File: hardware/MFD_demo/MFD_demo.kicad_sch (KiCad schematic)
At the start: 52 parts, among them J1 Pins_Ard, J2 POWER, Q1 IRF740, Q10 IRF740, Q2 IRF740, Q3 IRF740, Q4 IRF740, Q5 IRF740, Q6 IRF740, Q7 IRF740, Q8 IRF740, Q9 IRF740

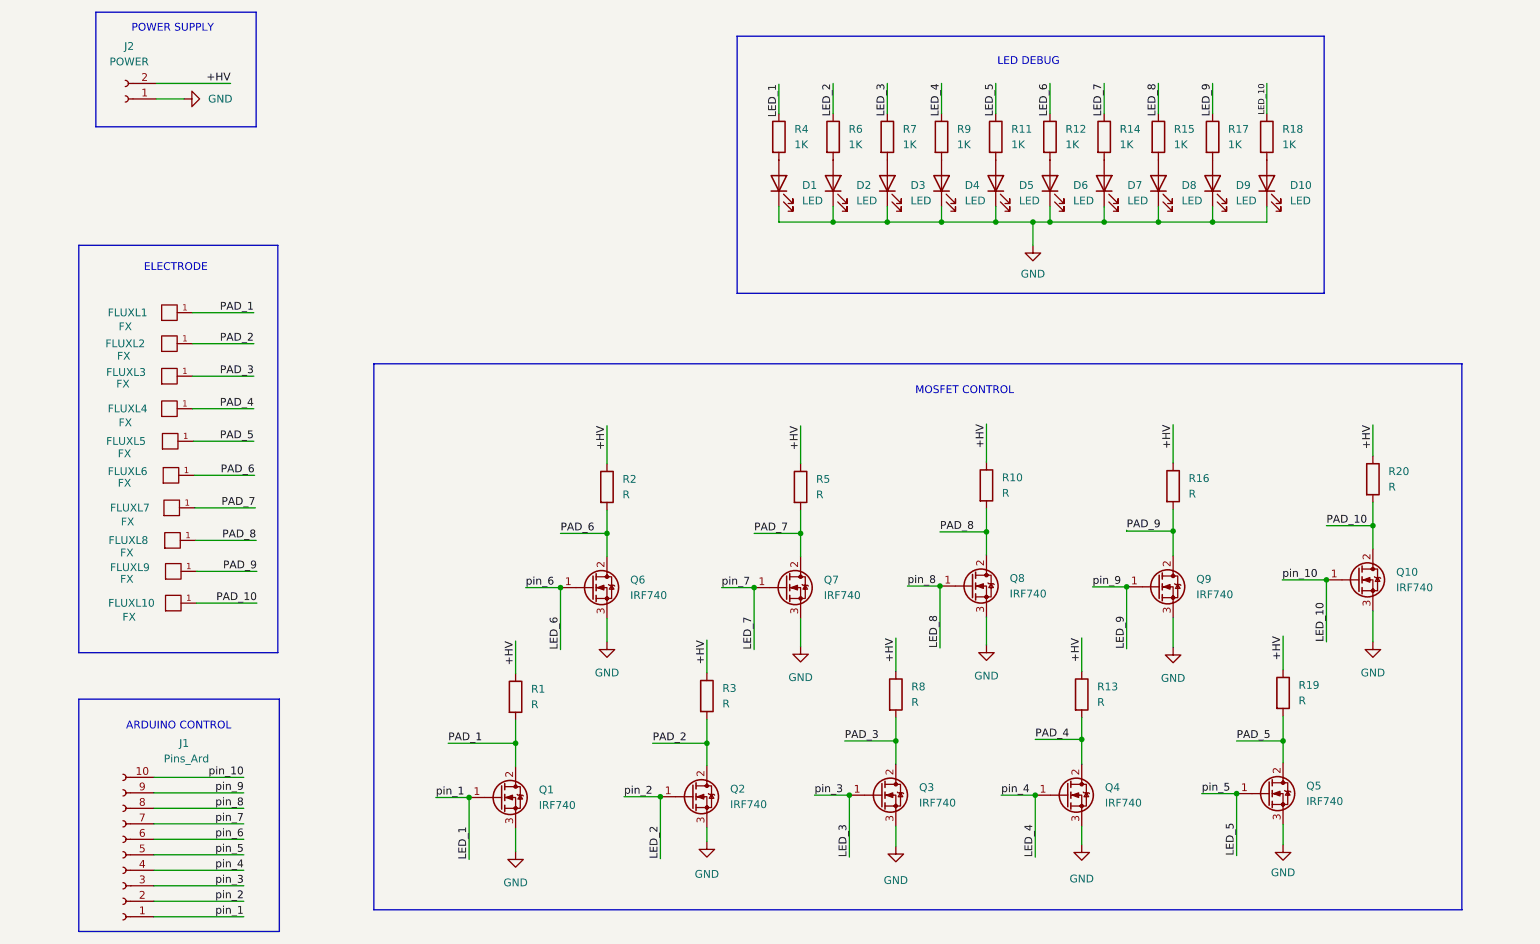
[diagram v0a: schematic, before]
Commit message: Update schem + layout PCB: Changes from 10 electrodes -> 6 electrodes
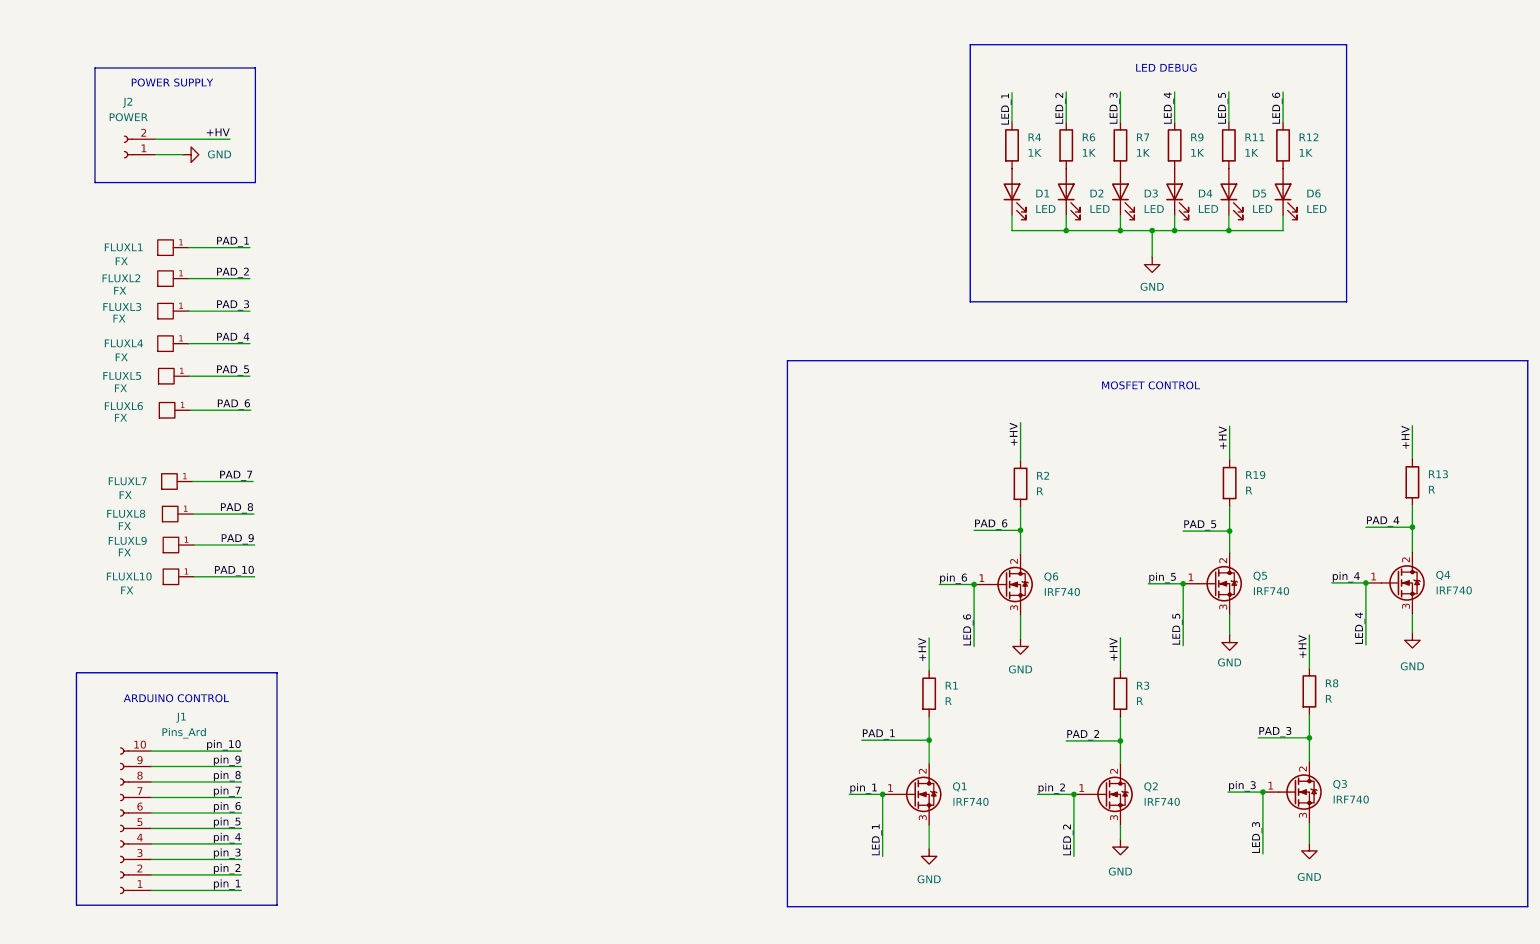
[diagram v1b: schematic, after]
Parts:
- removed D10, D7, D8, D9: LED, LED_THT:LED_D4.0mm, symbol Device:LED
- removed Q10, Q7, Q8, Q9: IRF740, Package_TO_SOT_THT:TO-220-3_Vertical, symbol Transistor_FET:IRF740
- removed R10, R16, R20, R5: R, Resistor_THT:R_Axial_DIN0207_L6.3mm_D2.5mm_P10.16mm_Horizontal, symbol Device:R
- removed R14, R15, R17, R18: 1K, Resistor_THT:R_Axial_DIN0207_L6.3mm_D2.5mm_P10.16mm_Horizontal, symbol Device:R
- D1, D2, D3, D4, D5, D6: footprint LED_THT:LED_D4.0mm -> LED_THT:LED_D5.0mm_IRBlack
- R1, R11, R12, R13, R19, R2, R3, R4, R6, R7, R8, R9: footprint Resistor_THT:R_Axial_DIN0207_L6.3mm_D2.5mm_P10.16mm_Horizontal -> Resistor_THT:R_Axial_DIN0204_L3.6mm_D1.6mm_P5.08mm_Horizontal
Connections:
- net LED_10 renamed pin_10
- net LED_7 renamed pin_7
- net LED_8 renamed pin_8
- net LED_9 renamed pin_9
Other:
- note removed: "ELECTRODE"
- moved on the sheet: D1, D2, D3, D4, D5, D6, FLUXL1, FLUXL10, FLUXL2, FLUXL3, FLUXL4, FLUXL5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

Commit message: Update PCB layout version 01
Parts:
- removed J1: Pins_Ard, Connector_PinHeader_2.54mm:PinHeader_1x10_P2.54mm_Vertical, symbol Connector:Conn_01x10_Female
- added J1, J3: GND_Electrodes, Connector_PinSocket_2.54mm:PinSocket_1x01_P2.54mm_Vertical, symbol Connector:Conn_01x01_Female
- added J10: GND, Connector_PinSocket_2.54mm:PinSocket_1x03_P2.54mm_Vertical, symbol Connector:Conn_01x03_Female
- added J4: Ard_1, Connector_PinSocket_2.54mm:PinSocket_1x01_P2.54mm_Vertical, symbol Connector:Conn_01x01_Female
- added J5: Ard_2, Connector_PinSocket_2.54mm:PinSocket_1x01_P2.54mm_Vertical, symbol Connector:Conn_01x01_Female
- added J6: Ard_3, Connector_PinSocket_2.54mm:PinSocket_1x01_P2.54mm_Vertical, symbol Connector:Conn_01x01_Female
- added J7: Ard_4, Connector_PinSocket_2.54mm:PinSocket_1x01_P2.54mm_Vertical, symbol Connector:Conn_01x01_Female
- added J8: Ard_5, Connector_PinSocket_2.54mm:PinSocket_1x01_P2.54mm_Vertical, symbol Connector:Conn_01x01_Female
- added J9: Ard_6, Connector_PinSocket_2.54mm:PinSocket_1x01_P2.54mm_Vertical, symbol Connector:Conn_01x01_Female
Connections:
- net PAD_8 is gone; now on an unnamed net: FLUXL8.1
- net PAD_9 is gone; now on an unnamed net: FLUXL9.1
- net GND: now also J10.1 (Pin_1), J10.2 (Pin_2), J10.3 (Pin_3)
- net LED_1: now also J4.1 (Pin_1)
- net LED_2: now also J5.1 (Pin_1)
- net LED_3: now also J6.1 (Pin_1)
- net LED_4: now also J7.1 (Pin_1)
- net LED_5: now also J8.1 (Pin_1)
- net LED_6: now also J9.1 (Pin_1)
- net PAD_10: no longer names the net of FLUXL10.1
- net PAD_10: now also J3.1 (Pin_1)
- net PAD_7: no longer names the net of FLUXL7.1
- net PAD_7: now also J1.1 (Pin_1)
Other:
- note added: "ELECTRODES"
- moved on the sheet: D1, D2, D3, D4, D5, D6, FLUXL1, FLUXL10, FLUXL2, FLUXL3, FLUXL4, FLUXL5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

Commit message: Update PCB layout
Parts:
- R1, R11, R12, R13, R19, R2, R3, R4, R6, R7, R8, R9: footprint Resistor_THT:R_Axial_DIN0204_L3.6mm_D1.6mm_P5.08mm_Horizontal -> Resistor_THT:R_Axial_DIN0207_L6.3mm_D2.5mm_P10.16mm_Horizontal
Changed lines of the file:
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@@
       (effects (font (size 1.27 1.27)) (justify left))
     )
-    (property "Footprint" "Resistor_THT:R_Axial_DIN0204_L3.6mm_D1.6mm_P5.08mm_Horizontal" (id 2) (at 169.545 128.905 90)
+    (property "Footprint" "Resistor_THT:R_Axial_DIN0207_L6.3mm_D2.5mm_P10.16mm_Horizontal" (id 2) (at 169.545 128.905 90)
       (effects (font (size 1.27 1.27)) hide)
     )
@@
       (effects (font (size 1.27 1.27)) (justify left))
     )
-    (property "Footprint" "Resistor_THT:R_Axial_DIN0204_L3.6mm_D1.6mm_P5.08mm_Horizontal" (id 2) (at 154.051 94.107 90)
+    (property "Footprint" "Resistor_THT:R_Axial_DIN0207_L6.3mm_D2.5mm_P10.16mm_Horizontal" (id 2) (at 154.051 94.107 90)
       (effects (font (size 1.27 1.27)) hide)
     )
@@
       (effects (font (size 1.27 1.27)) (justify left))
     )
-    (property "Footprint" "Resistor_THT:R_Axial_DIN0204_L3.6mm_D1.6mm_P5.08mm_Horizontal" (id 2) (at 203.962 128.905 90)
+    (property "Footprint" "Resistor_THT:R_Axial_DIN0207_L6.3mm_D2.5mm_P10.16mm_Horizontal" (id 2) (at 203.962 128.905 90)
       (effects (font (size 1.27 1.27)) hide)
     )
@@
       (effects (font (size 1.27 1.27)) (justify left))
     )
-    (property "Footprint" "Resistor_THT:R_Axial_DIN0204_L3.6mm_D1.6mm_P5.08mm_Horizontal" (id 2) (at 189.357 94.107 90)
+    (property "Footprint" "Resistor_THT:R_Axial_DIN0207_L6.3mm_D2.5mm_P10.16mm_Horizontal" (id 2) (at 189.357 94.107 90)
       (effects (font (size 1.27 1.27)) hide)
     )
@@
       (effects (font (size 1.27 1.27)) (justify left))
     )
-    (property "Footprint" "Resistor_THT:R_Axial_DIN0204_L3.6mm_D1.6mm_P5.08mm_Horizontal" (id 2) (at 181.356 41.402 90)
+    (property "Footprint" "Resistor_THT:R_Axial_DIN0207_L6.3mm_D2.5mm_P10.16mm_Horizontal" (id 2) (at 181.356 41.402 90)
       (effects (font (size 1.27 1.27)) hide)
     )
@@
       (effects (font (size 1.27 1.27)) (justify left))
     )
-    (property "Footprint" "Resistor_THT:R_Axial_DIN0204_L3.6mm_D1.6mm_P5.08mm_Horizontal" (id 2) (at 154.686 41.402 90)
+    (property "Footprint" "Resistor_THT:R_Axial_DIN0207_L6.3mm_D2.5mm_P10.16mm_Horizontal" (id 2) (at 154.686 41.402 90)
       (effects (font (size 1.27 1.27)) hide)
     )
@@
       (effects (font (size 1.27 1.27)) (justify left))
     )
-    (property "Footprint" "Resistor_THT:R_Axial_DIN0204_L3.6mm_D1.6mm_P5.08mm_Horizontal" (id 2) (at 223.647 94.107 90)
+    (property "Footprint" "Resistor_THT:R_Axial_DIN0207_L6.3mm_D2.5mm_P10.16mm_Horizontal" (id 2) (at 223.647 94.107 90)
       (effects (font (size 1.27 1.27)) hide)
     )
@@
       (effects (font (size 1.27 1.27)) (justify left))
     )
-    (property "Footprint" "Resistor_THT:R_Axial_DIN0204_L3.6mm_D1.6mm_P5.08mm_Horizontal" (id 2) (at 172.466 41.402 90)
+    (property "Footprint" "Resistor_THT:R_Axial_DIN0207_L6.3mm_D2.5mm_P10.16mm_Horizontal" (id 2) (at 172.466 41.402 90)
       (effects (font (size 1.27 1.27)) hide)
     )
@@
       (effects (font (size 1.27 1.27)) (justify left))
     )
-    (property "Footprint" "Resistor_THT:R_Axial_DIN0204_L3.6mm_D1.6mm_P5.08mm_Horizontal" (id 2) (at 136.906 41.402 90)
+    (property "Footprint" "Resistor_THT:R_Axial_DIN0207_L6.3mm_D2.5mm_P10.16mm_Horizontal" (id 2) (at 136.906 41.402 90)
       (effects (font (size 1.27 1.27)) hide)
     )
@@
       (effects (font (size 1.27 1.27)) (justify left))
     )
-    (property "Footprint" "Resistor_THT:R_Axial_DIN0204_L3.6mm_D1.6mm_P5.08mm_Horizontal" (id 2) (at 137.16 128.524 90)
+    (property "Footprint" "Resistor_THT:R_Axial_DIN0207_L6.3mm_D2.5mm_P10.16mm_Horizontal" (id 2) (at 137.16 128.524 90)
       (effects (font (size 1.27 1.27)) hide)
     )
@@
       (effects (font (size 1.27 1.27)) (justify left))
     )
-    (property "Footprint" "Resistor_THT:R_Axial_DIN0204_L3.6mm_D1.6mm_P5.08mm_Horizontal" (id 2) (at 145.796 41.402 90)
+    (property "Footprint" "Resistor_THT:R_Axial_DIN0207_L6.3mm_D2.5mm_P10.16mm_Horizontal" (id 2) (at 145.796 41.402 90)
       (effects (font (size 1.27 1.27)) hide)
     )
@@
       (effects (font (size 1.27 1.27)) (justify left))
     )
-    (property "Footprint" "Resistor_THT:R_Axial_DIN0204_L3.6mm_D1.6mm_P5.08mm_Horizontal" (id 2) (at 163.576 41.402 90)
+    (property "Footprint" "Resistor_THT:R_Axial_DIN0207_L6.3mm_D2.5mm_P10.16mm_Horizontal" (id 2) (at 163.576 41.402 90)
       (effects (font (size 1.27 1.27)) hide)
     )
@@
     )
     (path "/be0a93d4-c7fe-4417-b63d-cae7dd23acfb"
-      (reference "R1") (unit 1) (value "R") (footprint "Resistor_THT:R_Axial_DIN0204_L3.6mm_D1.6mm_P5.08mm_Horizontal")
+      (reference "R1") (unit 1) (value "R") (footprint "Resistor_THT:R_Axial_DIN0207_L6.3mm_D2.5mm_P10.16mm_Horizontal")
     )
     (path "/27ad1b76-a7b6-4284-b8ed-9188bd611cd9"
-      (reference "R2") (unit 1) (value "R") (footprint "Resistor_THT:R_Axial_DIN0204_L3.6mm_D1.6mm_P5.08mm_Horizontal")
+      (reference "R2") (unit 1) (value "R") (footprint "Resistor_THT:R_Axial_DIN0207_L6.3mm_D2.5mm_P10.16mm_Horizontal")
     )
     (path "/05d574de-583c-416b-a316-989f3cd535f3"
-      (reference "R3") (unit 1) (value "R") (footprint "Resistor_THT:R_Axial_DIN0204_L3.6mm_D1.6mm_P5.08mm_Horizontal")
+      (reference "R3") (unit 1) (value "R") (footprint "Resistor_THT:R_Axial_DIN0207_L6.3mm_D2.5mm_P10.16mm_Horizontal")
     )
     (path "/b710cd78-0899-47ec-87c6-6995f4acff0d"
-      (reference "R4") (unit 1) (value "1K") (footprint "Resistor_THT:R_Axial_DIN0204_L3.6mm_D1.6mm_P5.08mm_Horizontal")
+      (reference "R4") (unit 1) (value "1K") (footprint "Resistor_THT:R_Axial_DIN0207_L6.3mm_D2.5mm_P10.16mm_Horizontal")
     )
     (path "/e09b8ead-9636-4a68-a80a-e4f72d0a1616"
-      (reference "R6") (unit 1) (value "1K") (footprint "Resistor_THT:R_Axial_DIN0204_L3.6mm_D1.6mm_P5.08mm_Horizontal")
+      (reference "R6") (unit 1) (value "1K") (footprint "Resistor_THT:R_Axial_DIN0207_L6.3mm_D2.5mm_P10.16mm_Horizontal")
     )
     (path "/8f5749bc-b397-4181-990f-91932b53985e"
-      (reference "R7") (unit 1) (value "1K") (footprint "Resistor_THT:R_Axial_DIN0204_L3.6mm_D1.6mm_P5.08mm_Horizontal")
+      (reference "R7") (unit 1) (value "1K") (footprint "Resistor_THT:R_Axial_DIN0207_L6.3mm_D2.5mm_P10.16mm_Horizontal")
     )
     (path "/45570490-597d-42e6-ab7e-3269a77d63b4"
-      (reference "R8") (unit 1) (value "R") (footprint "Resistor_THT:R_Axial_DIN0204_L3.6mm_D1.6mm_P5.08mm_Horizontal")
+      (reference "R8") (unit 1) (value "R") (footprint "Resistor_THT:R_Axial_DIN0207_L6.3mm_D2.5mm_P10.16mm_Horizontal")
     )
     (path "/e3976c00-518b-4fdf-bdaf-5cbde63a2a9e"
-      (reference "R9") (unit 1) (value "1K") (footprint "Resistor_THT:R_Axial_DIN0204_L3.6mm_D1.6mm_P5.08mm_Horizontal")
+      (reference "R9") (unit 1) (value "1K") (footprint "Resistor_THT:R_Axial_DIN0207_L6.3mm_D2.5mm_P10.16mm_Horizontal")
     )
     (path "/aac22eac-a078-45d9-8bc1-9712e010cf3f"
-      (reference "R11") (unit 1) (value "1K") (footprint "Resistor_THT:R_Axial_DIN0204_L3.6mm_D1.6mm_P5.08mm_Horizontal")
+      (reference "R11") (unit 1) (value "1K") (footprint "Resistor_THT:R_Axial_DIN0207_L6.3mm_D2.5mm_P10.16mm_Horizontal")
     )
     (path "/76c9ee3e-8eff-43c3-8c23-922c0f01789b"
-      (reference "R12") (unit 1) (value "1K") (footprint "Resistor_THT:R_Axial_DIN0204_L3.6mm_D1.6mm_P5.08mm_Horizontal")
+      (reference "R12") (unit 1) (value "1K") (footprint "Resistor_THT:R_Axial_DIN0207_L6.3mm_D2.5mm_P10.16mm_Horizontal")
     )
     (path "/a00fc1c5-f91b-4fd1-a923-7db550af0d65"
-      (reference "R13") (unit 1) (value "R") (footprint "Resistor_THT:R_Axial_DIN0204_L3.6mm_D1.6mm_P5.08mm_Horizontal")
+      (reference "R13") (unit 1) (value "R") (footprint "Resistor_THT:R_Axial_DIN0207_L6.3mm_D2.5mm_P10.16mm_Horizontal")
     )
     (path "/6f29a0e0-685e-4409-9450-c55658860f84"
-      (reference "R19") (unit 1) (value "R") (footprint "Resistor_THT:R_Axial_DIN0204_L3.6mm_D1.6mm_P5.08mm_Horizontal")
-    )
-  )
+      (reference "R19") (unit 1) (value "R") (footprint "Resistor_THT:R_Axial_DIN0207_L6.3mm_D2.5mm_P10.16mm_Horizontal")
+    )
+  )
